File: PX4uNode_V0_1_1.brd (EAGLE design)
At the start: 45.4 x 34 mm, 130 parts, among them M3_MOUNT1101 MOUNT-HOLE3.1MM, M3_MOUNT1102 MOUNT-HOLE3.1MM, M3_MOUNT1103 MOUNT-HOLE3.1MM, M3_MOUNT1104 MOUNT-HOLE3.1MM, U101 STM32F4X7VX, U401 MAX3051, U402 MAX3051, X101 3.2x2.5 mm / 24 MHz / 15 ppm

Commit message: Nice and tidy
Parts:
- moved OSHW_LOGO 54.7 mm to (25.7, 24.8), flipped to the bottom
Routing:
- net SPI_INT_MISO: track 12.8 -> 10.1 mm
- net PPM_INPUT: track 32.1 -> 29.7 mm, vias 3 -> 2
- net FMU-USART2_CTS: track 16.2 -> 17.0 mm
- net FMU-USART3_TX: track 29.9 -> 29.3 mm
- net FMU-CH7: track 15.7 -> 15.0 mm
- net MAG_DRDY: track 16.4 -> 15.8 mm
- net VDD_3V3_SENSORS_EN: track 23.3 -> 22.8 mm, vias 4 -> 3
- net FMU-USART3_CTS: vias 4 -> 3

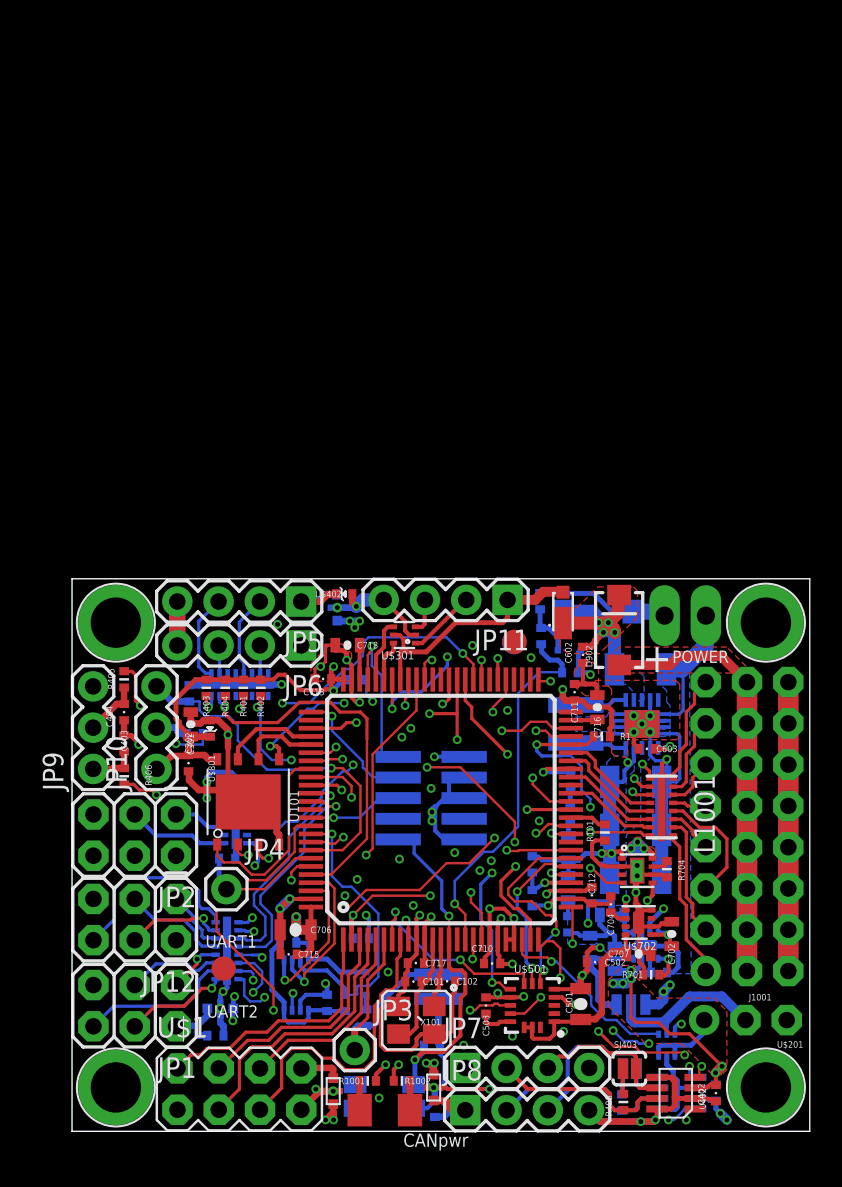
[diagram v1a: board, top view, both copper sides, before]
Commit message: Added more vias to regulator power paths
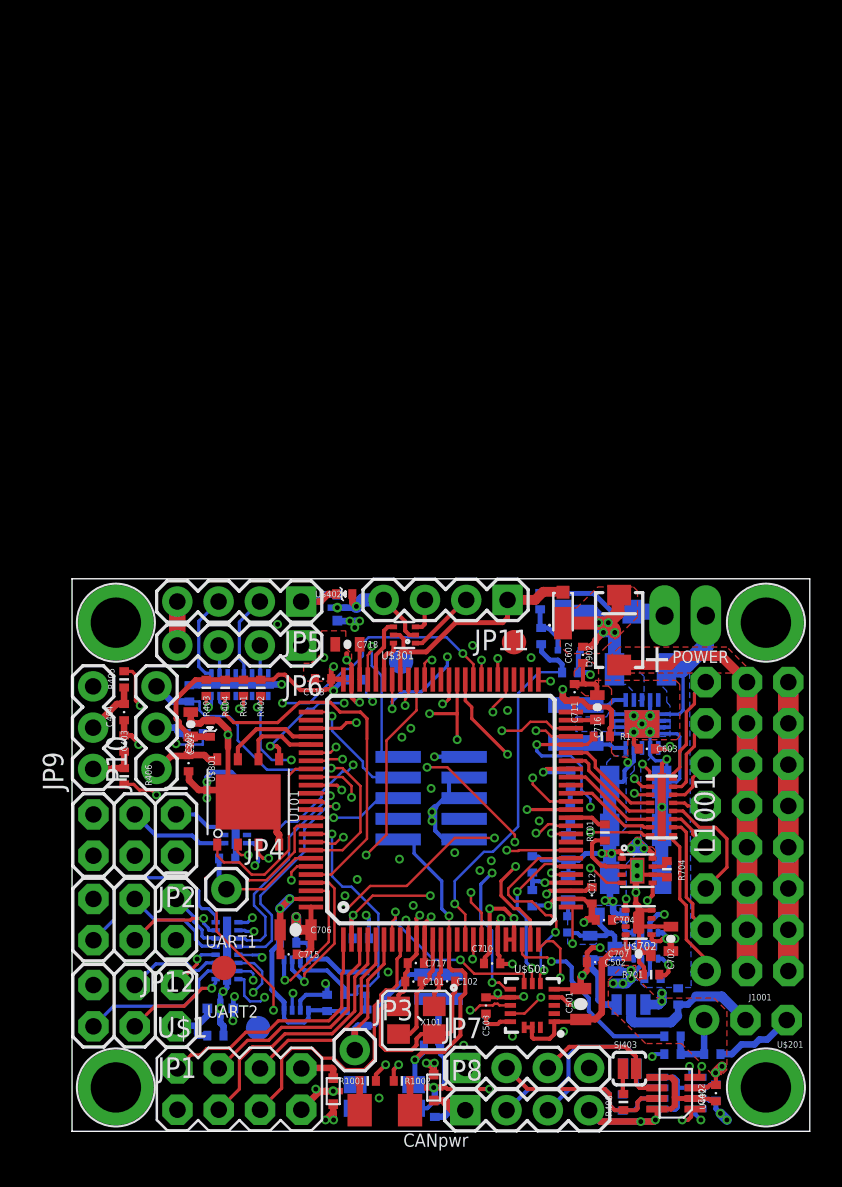
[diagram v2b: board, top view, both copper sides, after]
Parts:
- added JP13: FIDUCIAL1.5X3, pixhawk2:FIDUCIAL-1.5X3
- added R4, R5: 120R, pixhawk2:0402-RES
- added U$5: PESD0402-140, pixhawk2:0402-TVS
- U$3: value NUF2042XV6 -> PESD0402-140; device PX4lite:SOT563-6 -> pixhawk2:0402-TVS
- moved JP1102 7.05 mm to (33.0, 33.1)
- moved U$3 2.85 mm to (52.2, 8.95), turned to 180 degrees
- moved C704 1.05 mm to (45.5, 17.2), turned to 180 degrees
- moved C703 0.53 mm to (48.5, 13.6)
- moved C702 0.30 mm to (49.7, 16.0)
- moved R407 0.05 mm to (46.7, 5.97)
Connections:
- net GND: now also U$3.A, U$5.A; no longer U$3.2
- net N$18: now also U$5.C; no longer U$3.5
- net N$2: now also R4.P$2, R5.P$2, U$3.C; no longer U$3.1, U$3.3
- net PPM_INPUT: now also R4.P$1; no longer U$3.4
- net SPEKTRUM_RX: now also R5.P$1; no longer U$3.6
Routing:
- net FMU-VDD_3V3: track 91.3 -> 80.7 mm
- net GND: track 247.6 -> 243.2 mm, vias 29 -> 31
- net SPEKTRUM_RX: track 46.9 -> 42.8 mm, vias 6 -> 4
- net VDD_5V: track 31.5 -> 35.2 mm, vias 5 -> 7
- net PPM_INPUT: track 29.7 -> 30.8 mm
- net VDD_5V_PERIPH: track 93.2 -> 94.0 mm
- net CAN2_RX: track 34.1 -> 34.8 mm, vias 4 -> 2
- net N$2: track 5.17 -> 4.64 mm
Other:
- board text added: "DN"
- board text added: "DP"
- board text added: "GND"
- board text added: "VBUS"

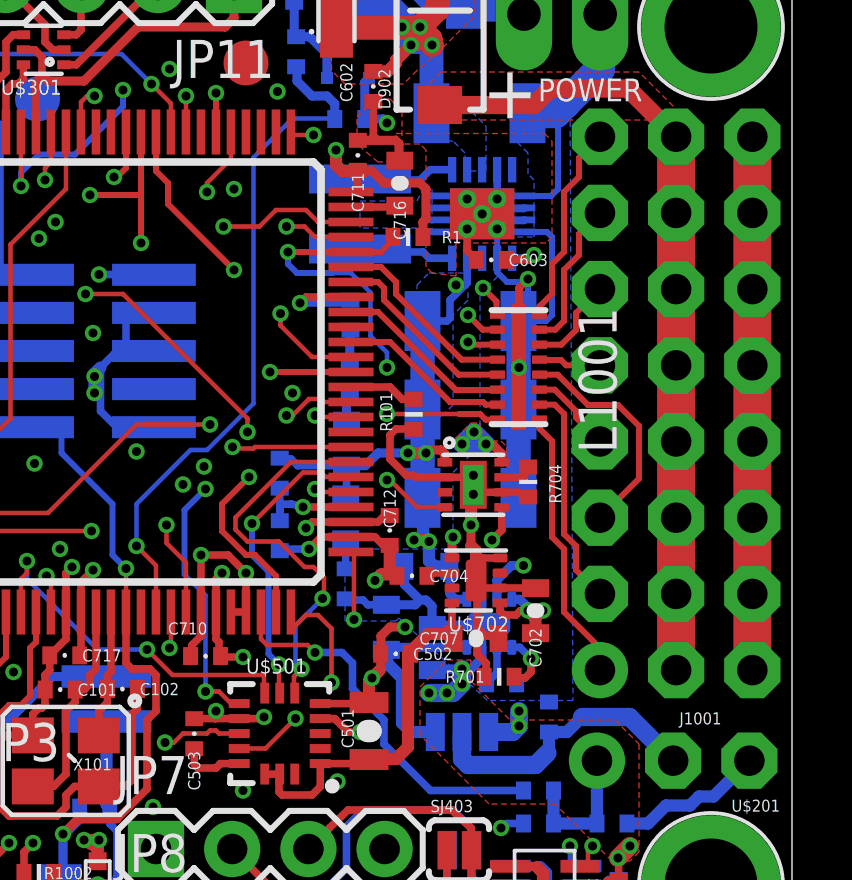
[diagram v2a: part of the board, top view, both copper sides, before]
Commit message: All design rules violations fixed or approved
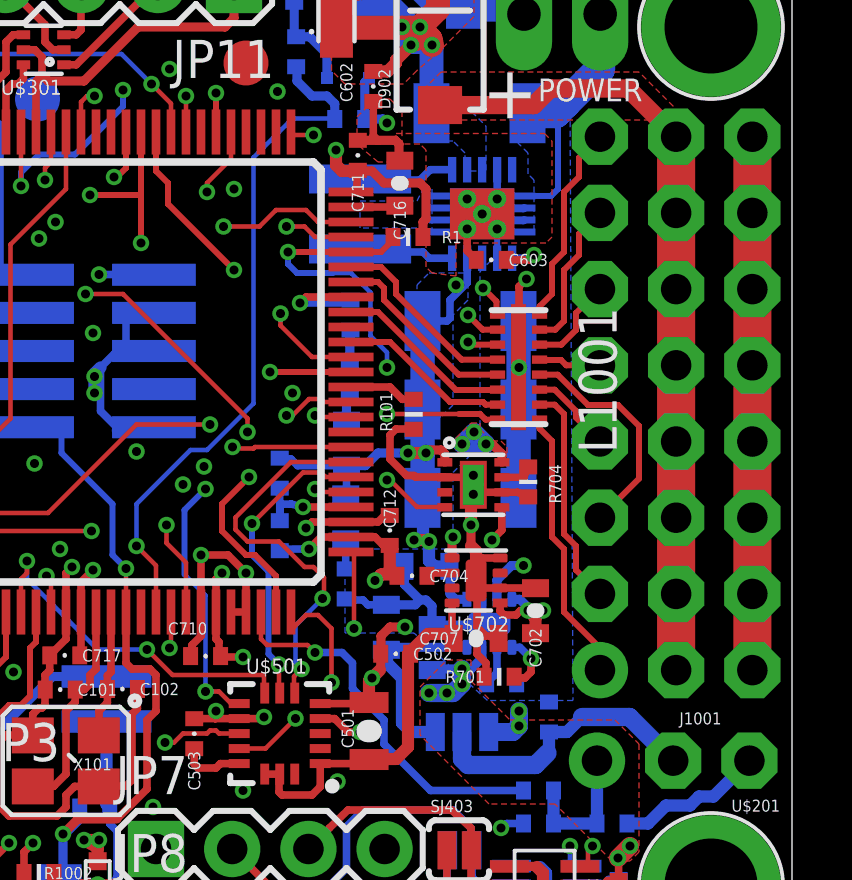
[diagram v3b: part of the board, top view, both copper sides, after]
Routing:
- net GND: track 243.2 -> 236.5 mm
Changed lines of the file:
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@@
 <layer number="14" name="Vertical" color="14" fill="15" visible="no" active="yes"/>
 <layer number="15" name="Power" color="11" fill="15" visible="no" active="yes"/>
-<layer number="16" name="Bottom" color="1" fill="1" visible="yes" active="yes"/>
+<layer number="16" name="Bottom" color="1" fill="1" visible="no" active="yes"/>
 <layer number="17" name="Pads" color="2" fill="1" visible="yes" active="yes"/>
 <layer number="18" name="Vias" color="2" fill="1" visible="yes" active="yes"/>
@@
 <layer number="20" name="Dimension" color="15" fill="1" visible="yes" active="yes"/>
 <layer number="21" name="tPlace" color="7" fill="1" visible="yes" active="yes"/>
-<layer number="22" name="bPlace" color="7" fill="1" visible="yes" active="yes"/>
+<layer number="22" name="bPlace" color="7" fill="1" visible="no" active="yes"/>
 <layer number="23" name="tOrigins" color="15" fill="1" visible="yes" active="yes"/>
-<layer number="24" name="bOrigins" color="15" fill="1" visible="yes" active="yes"/>
+<layer number="24" name="bOrigins" color="15" fill="1" visible="no" active="yes"/>
 <layer number="25" name="tNames" color="7" fill="1" visible="no" active="yes"/>
 <layer number="26" name="bNames" color="7" fill="1" visible="no" active="yes"/>
@@
 <layer number="38" name="bTest" color="7" fill="1" visible="no" active="yes"/>
 <layer number="39" name="tKeepout" color="4" fill="11" visible="yes" active="yes"/>
-<layer number="40" name="bKeepout" color="1" fill="11" visible="yes" active="yes"/>
+<layer number="40" name="bKeepout" color="1" fill="11" visible="no" active="yes"/>
 <layer number="41" name="tRestrict" color="4" fill="10" visible="yes" active="yes"/>
-<layer number="42" name="bRestrict" color="1" fill="10" visible="yes" active="yes"/>
+<layer number="42" name="bRestrict" color="1" fill="10" visible="no" active="yes"/>
 <layer number="43" name="vRestrict" color="2" fill="10" visible="no" active="yes"/>
 <layer number="44" name="Drills" color="7" fill="1" visible="no" active="yes"/>
@@
 <layer number="50" name="dxf" color="7" fill="1" visible="no" active="yes"/>
 <layer number="51" name="tDocu" color="7" fill="1" visible="yes" active="yes"/>
-<layer number="52" name="bDocu" color="7" fill="1" visible="yes" active="yes"/>
+<layer number="52" name="bDocu" color="7" fill="1" visible="no" active="yes"/>
 <layer number="53" name="tGND_GNDA" color="7" fill="9" visible="no" active="no"/>
 <layer number="54" name="bGND_GNDA" color="1" fill="9" visible="no" active="no"/>
@@
 <wire x1="43.2" y1="16.25" x2="43.2" y2="19.5" width="0.1524" layer="14"/>
 <wire x1="43.05" y1="16.1" x2="43.2" y2="16.25" width="0.1524" layer="14"/>
-<wire x1="43.05" y1="15.3" x2="43.05" y2="16.1" width="0.1524" layer="14"/>
-<wire x1="43.65" y1="14.7" x2="43.05" y2="15.3" width="0.1524" layer="14"/>
-<wire x1="43.65" y1="12.7" x2="43.65" y2="14.7" width="0.1524" layer="14"/>
+<wire x1="43.05" y1="15.2" x2="43.05" y2="16.1" width="0.1524" layer="14"/>
+<wire x1="43.65" y1="14.6" x2="43.05" y2="15.2" width="0.1524" layer="14"/>
+<wire x1="43.65" y1="12.7" x2="43.65" y2="14.6" width="0.1524" layer="14"/>
 <wire x1="43.8" y1="12" x2="43.8" y2="12.55" width="0.1524" layer="14"/>
 <wire x1="43.8" y1="12.55" x2="43.65" y2="12.7" width="0.1524" layer="14"/>
@@
 <contactref element="D1" pad="A"/>
 <wire x1="49.0848" y1="22.7512" x2="49.0848" y2="25.6976" width="0.8128" layer="16"/>
-<via x="49.4" y="27.1" extent="1-16" drill="0.3"/>
+<via x="49.35" y="27.1" extent="1-16" drill="0.3"/>
 <contactref element="U$1" pad="7"/>
 <wire x1="52.4216" y1="6.0496" x2="52.1504" y2="6.0496" width="0.254" layer="1"/>
@@
 <wire x1="50.4" y1="30.1" x2="50.4" y2="32.7" width="0.2" layer="16"/>
 <wire x1="50.4" y1="32.7" x2="50.65" y2="32.95" width="0.2" layer="16"/>
-<wire x1="49.297" y1="28.668" x2="50.032" y2="28.668" width="0.2" layer="16"/>
-<wire x1="50.032" y1="28.668" x2="50.2" y2="28.5" width="0.2" layer="16"/>
-<wire x1="50.2" y1="28.5" x2="50.2" y2="25.9" width="0.2" layer="16"/>
-<wire x1="50.2" y1="25.9" x2="50" y2="25.7" width="0.2" layer="16"/>
-<wire x1="50" y1="25.7" x2="49.0872" y2="25.7" width="0.2" layer="16"/>
-<wire x1="49.0872" y1="25.7" x2="49.0848" y2="25.6976" width="0.2" layer="16"/>
-<wire x1="48.372" y1="27.793" x2="48.372" y2="27.328" width="0.2" layer="16"/>
-<wire x1="48.372" y1="27.328" x2="48.7" y2="27" width="0.2" layer="16"/>
-<wire x1="48.7" y1="27" x2="49.1" y2="27" width="0.2" layer="16"/>
-<wire x1="49.1" y1="27" x2="49.4" y2="27.1" width="0.2" layer="16"/>
-<wire x1="49.4" y1="27.1" x2="49.4" y2="26.1128" width="0.2" layer="16"/>
-<wire x1="49.4" y1="26.1128" x2="49.0848" y2="25.6976" width="0.2" layer="16"/>
 <wire x1="48.372" y1="27.793" x2="48.372" y2="28.768" width="0.2" layer="16"/>
 <wire x1="47.6736" y1="27.7376" x2="47.372" y2="28.0392" width="0.254" layer="1"/>
@@
 <wire x1="48.372" y1="30.743" x2="48.372" y2="29.768" width="0.254" layer="16"/>
 <polygon width="0.15" layer="16">
-<vertex x="49.6" y="28.5"/>
+<vertex x="49.6" y="28.7"/>
 <vertex x="49.6" y="30.4"/>
 <vertex x="49.4" y="30.6"/>
@@
 <vertex x="50.9" y="13.05"/>
 <vertex x="48.05" y="13.05"/>
-<vertex x="45.1" y="15.8"/>
-<vertex x="45" y="15.7"/>
-<vertex x="43.3" y="15.7"/>
+<vertex x="45.6" y="15.3"/>
+<vertex x="43.3" y="15.3"/>
 <vertex x="43.3" y="18.1"/>
 <vertex x="46.9" y="18.1"/>
 <vertex x="46.9" y="20.65"/>
 <vertex x="47.8" y="21.55"/>
-<vertex x="47.8" y="26.6"/>
-<vertex x="48.4" y="27.2"/>
-<vertex x="48.4" y="28.5"/>
+<vertex x="47.8" y="27.35"/>
+<vertex x="48.4" y="27.95"/>
+<vertex x="48.4" y="28.7"/>
 </polygon>
 <wire x1="44.4668" y1="14.0668" x2="44.2" y2="13.8" width="0.4064" layer="1"/>
@@
 <wire x1="48.85" y1="5.6" x2="48.9" y2="5.6" width="0.254" layer="16"/>
 <wire x1="35.65" y1="22.05" x2="36.932" y2="22.16" width="0.254" layer="16"/>
-<wire x1="49.1" y1="26.8" x2="49.1" y2="24.2" width="0.254" layer="1"/>
-<wire x1="49.4" y1="27.1" x2="49.1" y2="26.8" width="0.254" layer="1"/>
+<wire x1="49.1" y1="26.85" x2="49.1" y2="24.2" width="0.254" layer="1"/>
+<wire x1="49.35" y1="27.1" x2="49.1" y2="26.85" width="0.254" layer="1"/>
 <wire x1="49.1" y1="24.2" x2="49.0848" y2="24.1608" width="0.254" layer="1"/>
 <wire x1="44.8" y1="21.1" x2="44.8" y2="21.9" width="0.254" layer="1"/>
@@
 <wire x1="44.3" y1="17.05" x2="44.5" y2="17.25" width="0.4064" layer="1"/>
 <wire x1="44.5" y1="17.25" x2="45" y2="17.25" width="0.4064" layer="1"/>
-<wire x1="46.447" y1="29.468" x2="47.3" y2="29.45" width="0" layer="19" extent="16-16"/>
+<wire x1="46.447" y1="29.468" x2="47.372" y2="29.468" width="0.2" layer="16"/>
+<wire x1="47.372" y1="29.468" x2="47.372" y2="29.768" width="0.2" layer="16"/>
 </signal>
 <signal name="N$4">
@@
 <polygon width="0.254" layer="15">
 <vertex x="47.55" y="22.15"/>
-<vertex x="50" y="22.15"/>
-<vertex x="50.7" y="21.45"/>
+<vertex x="50.7" y="22.15"/>
 <vertex x="50.7" y="12.35"/>
 <vertex x="50.65" y="12.3"/>
@@
 <vertex x="47" y="21.6"/>
 </polygon>
-<polygon width="0.2" layer="15">
+<polygon width="0.254" layer="15">
 <vertex x="46.9" y="21.4"/>
 <vertex x="50.7" y="21.45"/>
-<vertex x="50.85" y="22.9"/>
+<vertex x="50.85" y="21.6"/>
 <vertex x="50.85" y="30.75"/>
 <vertex x="45.55" y="36.05"/>
@@
 <wire x1="32.25" y1="14" x2="32.25" y2="8.95" width="0.1524" layer="14"/>
 <wire x1="34.15" y1="15.9" x2="32.25" y2="14" width="0.1524" layer="3"/>
-<wire x1="43.45" y1="15.9" x2="34.15" y2="15.9" width="0.1524" layer="3"/>
-<wire x1="43.6" y1="15.75" x2="43.45" y2="15.9" width="0.1524" layer="3"/>
-<wire x1="43.6" y1="18" x2="43.6" y2="15.75" width="0.1524" layer="1"/>
+<wire x1="43.15" y1="15.9" x2="34.15" y2="15.9" width="0.1524" layer="3"/>
+<wire x1="43.6" y1="15.45" x2="43.15" y2="15.9" width="0.1524" layer="3"/>
+<wire x1="43.6" y1="18" x2="43.6" y2="15.45" width="0.1524" layer="1"/>
 <wire x1="43.5" y1="18" x2="43.6" y2="18" width="0.1524" layer="1"/>
 <via x="32.25" y="14" extent="1-16" drill="0.3"/>
-<via x="43.6" y="15.75" extent="1-16" drill="0.3"/>
+<via x="43.6" y="15.45" extent="1-16" drill="0.3"/>
 </signal>
 <signal name="N$19">

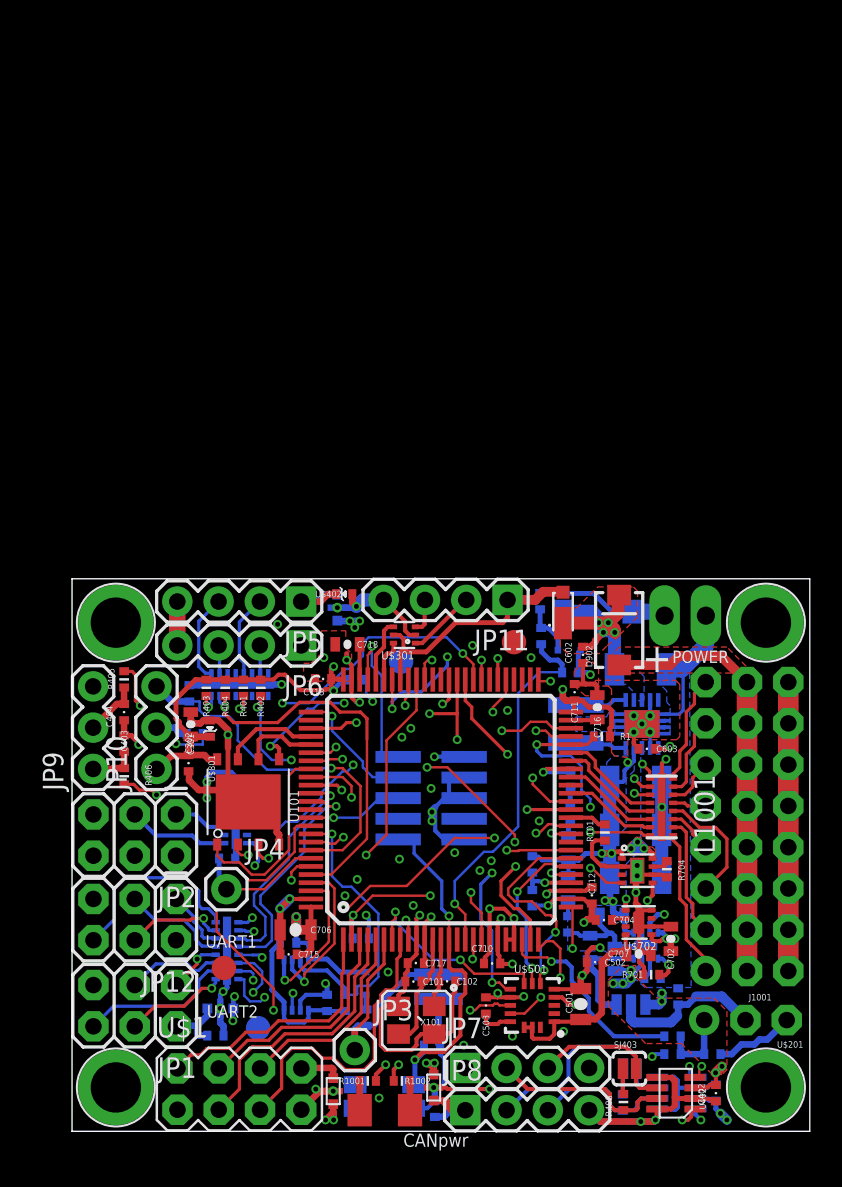
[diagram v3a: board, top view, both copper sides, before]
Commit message: Thickened pogo connector traces where possible
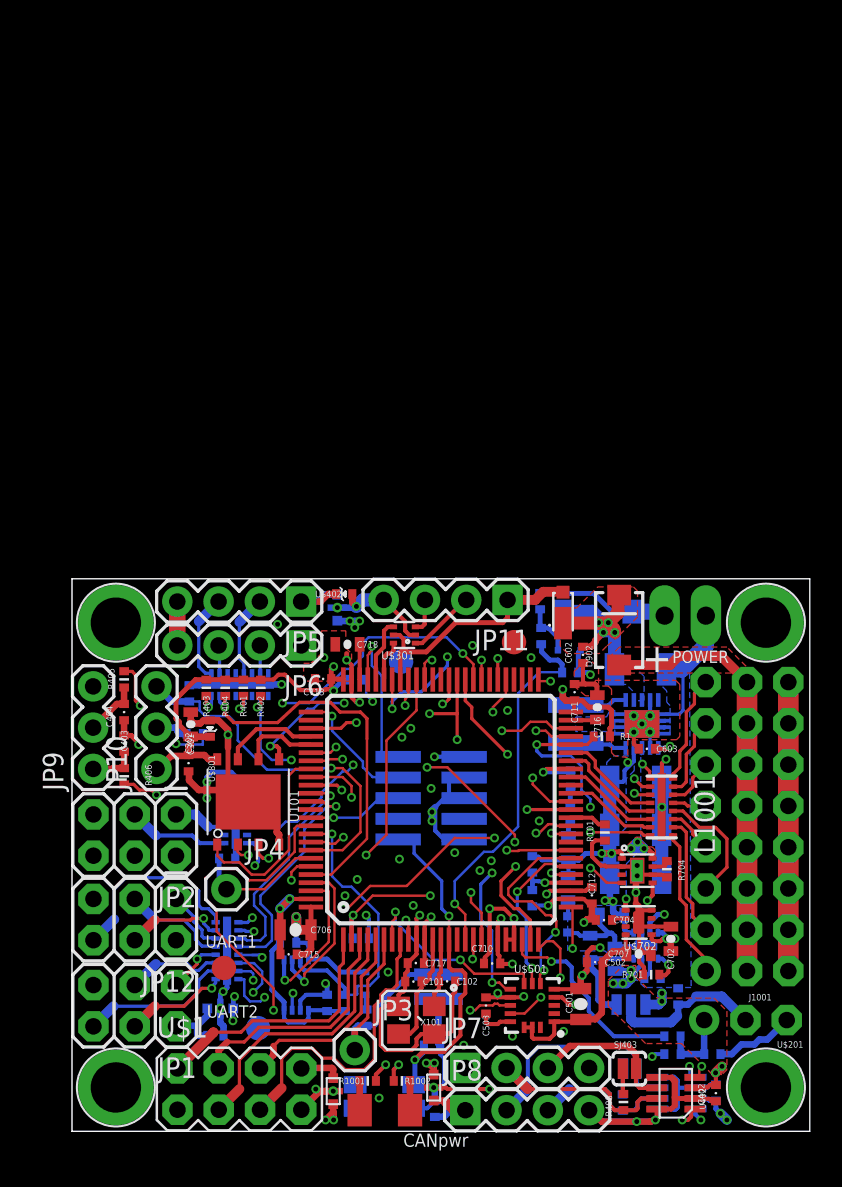
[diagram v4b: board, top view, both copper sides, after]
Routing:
- net !SPI_EXT_NSS: track 14.1 -> 14.7 mm
